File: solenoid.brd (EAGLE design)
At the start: 35.6 x 30.5 mm, 40 parts, among them Y1 ECS-80-S-4X

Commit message: Update solenoid.brd
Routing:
- net +3V3: track 59.1 -> 63.3 mm
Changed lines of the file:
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@@
 <wire x1="29.972" y1="12.148" x2="29.674" y2="12.148" width="0.254" layer="1"/>
 <wire x1="29.972" y1="10.922" x2="29.972" y2="12.148" width="0.254" layer="1"/>
-<wire x1="20.558" y1="19.288" x2="20.32" y2="19.05" width="0.254" layer="16"/>
-<wire x1="20.32" y1="19.05" x2="20.32" y2="18.542" width="0.254" layer="16"/>
-<via x="20.32" y="18.542" extent="1-16" drill="0.35"/>
-<wire x1="20.32" y1="18.542" x2="20.32" y2="18.034" width="0.254" layer="1"/>
-<wire x1="20.32" y1="18.034" x2="20.606" y2="17.748" width="0.254" layer="1"/>
+<via x="20.066" y="18.542" extent="1-16" drill="0.35"/>
+<wire x1="20.066" y1="18.542" x2="20.066" y2="18.288" width="0.254" layer="1"/>
+<wire x1="20.066" y1="18.288" x2="20.606" y2="17.748" width="0.254" layer="1"/>
 <wire x1="20.606" y1="17.748" x2="21.174" y2="17.748" width="0.254" layer="1"/>
 <wire x1="31.558" y1="10.506" x2="30.388" y2="10.506" width="0.254" layer="1"/>
@@
 <via x="20.0084" y="11.95728125" extent="1-16" drill="0.35"/>
 <wire x1="22.86" y1="15.976" x2="22.606" y2="15.722" width="0.254" layer="16"/>
-<wire x1="22.606" y1="15.722" x2="22.606" y2="14.058" width="0.254" layer="16"/>
+<wire x1="22.606" y1="15.722" x2="22.606" y2="14.986" width="0.254" layer="16"/>
+<wire x1="22.606" y1="14.058" x2="22.606" y2="14.986" width="0.254" layer="16"/>
 <wire x1="22.606" y1="14.058" x2="20.0084" y2="14.058" width="0.254" layer="16"/>
 <wire x1="20.0084" y1="14.058" x2="19.138" y2="14.058" width="0.254" layer="16"/>
@@
 <wire x1="10.834" y1="20.74" x2="12.446" y2="22.352" width="0.254" layer="1"/>
 <wire x1="12.446" y1="22.352" x2="18.542" y2="22.352" width="0.254" layer="1"/>
+<wire x1="22.606" y1="14.986" x2="21.971" y2="15.621" width="0.254" layer="16"/>
+<wire x1="21.971" y1="15.621" x2="21.336" y2="15.621" width="0.254" layer="16"/>
+<wire x1="21.336" y1="15.621" x2="20.955" y2="16.002" width="0.254" layer="16"/>
+<wire x1="20.955" y1="16.002" x2="20.955" y2="17.653" width="0.254" layer="16"/>
+<wire x1="20.955" y1="17.653" x2="20.066" y2="18.542" width="0.254" layer="16"/>
 </signal>
 <signal name="GPIO1">
@@
 <wire x1="33.258" y1="10.506" x2="33.288" y2="10.476" width="0.254" layer="1"/>
 <wire x1="33.288" y1="10.476" x2="33.288" y2="8.836" width="0.254" layer="1"/>
-<wire x1="33.288" y1="8.836" x2="33.288" y2="8.58286875" width="0.254" layer="1"/>
 <wire x1="32.931" y1="12.984" x2="33.258" y2="12.657" width="0.254" layer="1"/>
 <wire x1="33.258" y1="12.657" x2="33.258" y2="10.506" width="0.254" layer="1"/>
@@
 <wire x1="32.687" y1="15.2689125" x2="32.687" y2="12.984" width="0.254" layer="1"/>
 <wire x1="30.734" y1="6.604" x2="32.131" y2="6.604" width="0.254" layer="1"/>
+<wire x1="32.131" y1="6.604" x2="33.288" y2="7.761" width="0.254" layer="1"/>
 <wire x1="33.288" y1="7.761" x2="33.288" y2="8.836" width="0.254" layer="1"/>
-<wire x1="32.131" y1="6.604" x2="33.288" y2="7.761" width="0.254" layer="1"/>
 </signal>
 <signal name="SWDIO">

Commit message: Update solenoid.brd
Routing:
- net SWCLK: track 7.57 -> 13.3 mm
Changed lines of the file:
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@@
 <wire x1="21.174" y1="11.2179125" x2="20.399" y2="10.4429125" width="0.254" layer="1"/>
 <wire x1="21.174" y1="11.2179125" x2="21.174" y2="12.148" width="0.254" layer="1"/>
-<wire x1="20.399" y1="8.3284" x2="20.574" y2="8.1534" width="0.254" layer="1"/>
-<wire x1="20.574" y1="8.1534" x2="20.96328125" y2="8.1534" width="0.254" layer="1"/>
-<wire x1="20.96328125" y1="8.1534" x2="22.51268125" y2="6.604" width="0.254" layer="1"/>
+<wire x1="20.574" y1="8.1534" x2="20.399" y2="8.3284" width="0.254" layer="1"/>
 <wire x1="20.399" y1="10.4429125" x2="20.399" y2="8.3284" width="0.254" layer="1"/>
-<wire x1="22.51268125" y1="6.604" x2="23.114" y2="6.604" width="0.254" layer="1"/>
+<wire x1="21.971" y1="4.064" x2="21.717" y2="4.318" width="0.254" layer="1"/>
+<wire x1="21.717" y1="4.318" x2="21.717" y2="7.493" width="0.254" layer="1"/>
+<wire x1="21.717" y1="7.493" x2="21.0566" y2="8.1534" width="0.254" layer="1"/>
+<wire x1="21.0566" y1="8.1534" x2="20.574" y2="8.1534" width="0.254" layer="1"/>
+<wire x1="23.114" y1="4.445" x2="23.368" y2="4.191" width="0.254" layer="1"/>
+<wire x1="23.368" y1="4.191" x2="23.241" y2="4.064" width="0.254" layer="1"/>
+<wire x1="23.114" y1="6.604" x2="23.114" y2="4.445" width="0.254" layer="1"/>
+<wire x1="23.241" y1="4.064" x2="21.971" y2="4.064" width="0.254" layer="1"/>
 </signal>
 <signal name="OSC_IN">

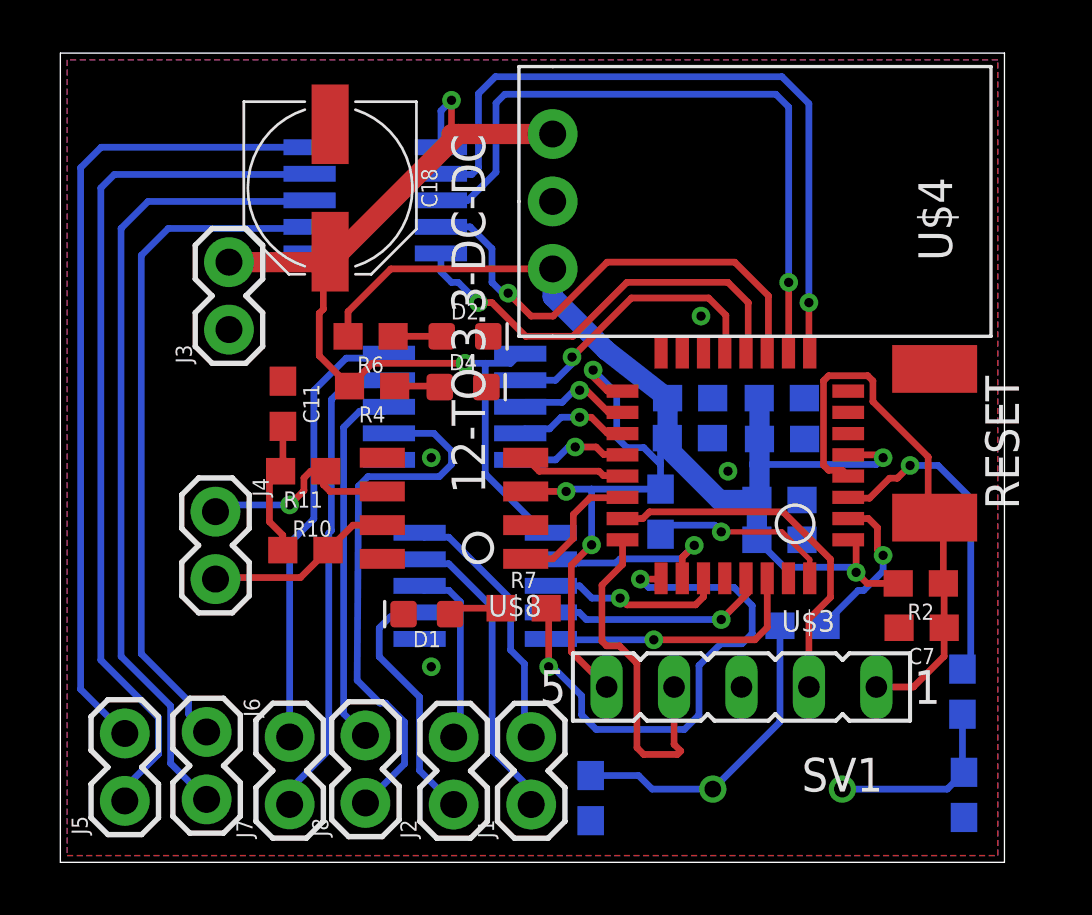
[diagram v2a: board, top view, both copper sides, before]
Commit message: small updates
finished making the wire impedances the same for oscillator and programming header, also made minor wire movements
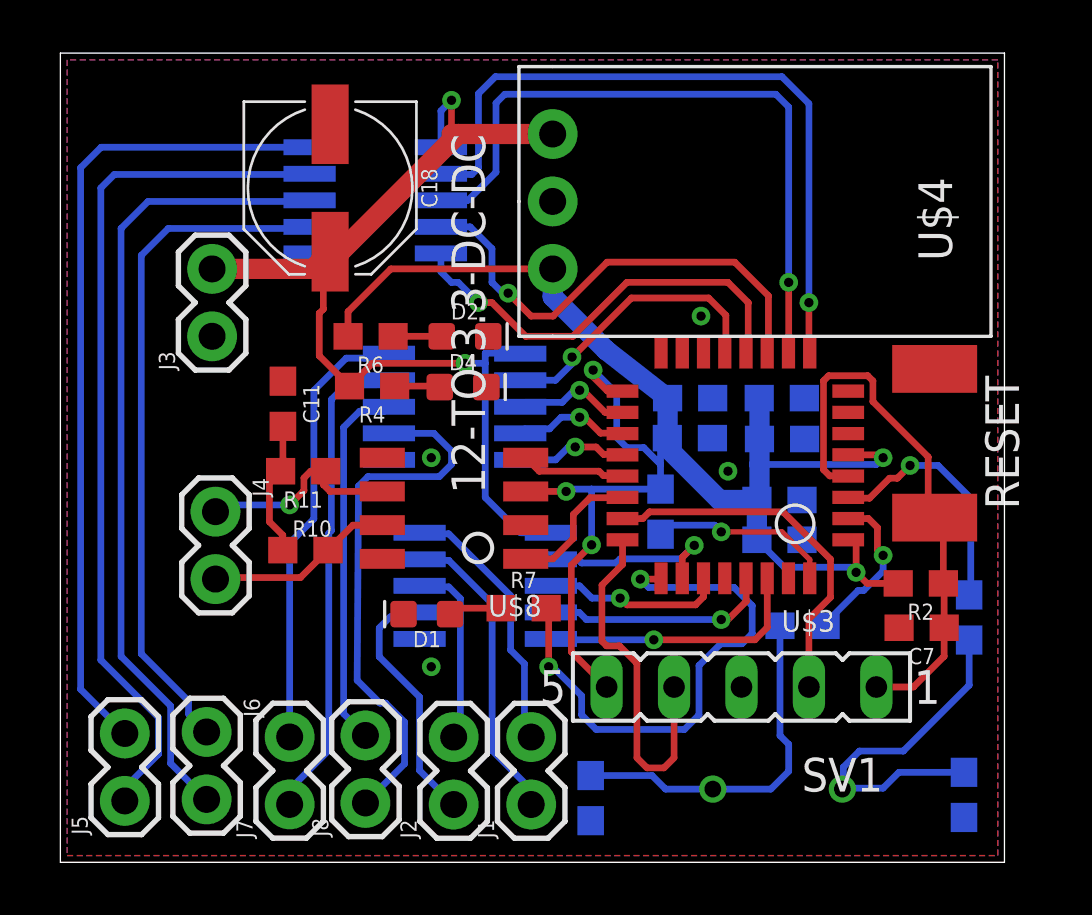
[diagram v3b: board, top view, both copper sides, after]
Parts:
- moved R1 2.81 mm to (34.2, 9.22)
- moved J3 0.68 mm to (5.71, 19.8)
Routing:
- net N$1: track 7.06 -> 13.4 mm
- net OSC_OUT: track 12.2 -> 9.32 mm
- net N$2: track 12.0 -> 13.6 mm
- net 12V: track 37.7 -> 39.2 mm

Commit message: Update solenoid.brd
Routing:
- net OSC_IN: track 6.05 -> 9.41 mm
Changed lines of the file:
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@@
 <contactref element="U$3" pad="PF0-OSC_IN"/>
 <contactref element="R3" pad="2"/>
-<wire x1="28.804" y1="8.91" x2="28.804" y2="8.992" width="0.254" layer="16"/>
-<wire x1="30.051" y1="10.239" x2="30.2549125" y2="10.239" width="0.254" layer="16"/>
 <wire x1="30.775" y1="12.609" x2="30.436" y2="12.948" width="0.254" layer="1"/>
 <wire x1="30.436" y1="12.948" x2="29.674" y2="12.948" width="0.254" layer="1"/>
-<wire x1="28.804" y1="8.992" x2="30.051" y2="10.239" width="0.254" layer="16"/>
-<wire x1="30.988" y1="10.9720875" x2="30.988" y2="11.562" width="0.254" layer="16"/>
+<wire x1="28.804" y1="8.91" x2="28.9259125" y2="8.91" width="0.254" layer="16"/>
 <via x="30.988" y="11.562" extent="1-16" drill="0.35"/>
 <wire x1="30.988" y1="11.562" x2="30.775" y2="11.775" width="0.254" layer="1"/>
 <wire x1="30.775" y1="11.775" x2="30.775" y2="12.609" width="0.254" layer="1"/>
-<wire x1="30.2549125" y1="10.239" x2="30.988" y2="10.9720875" width="0.254" layer="16"/>
+<wire x1="30.988" y1="11.562" x2="31.501" y2="11.049" width="0.254" layer="16"/>
+<wire x1="31.501" y1="11.049" x2="32.004" y2="11.049" width="0.254" layer="16"/>
+<wire x1="32.004" y1="11.049" x2="32.131" y2="10.922" width="0.254" layer="16"/>
+<wire x1="28.824" y1="8.89" x2="28.804" y2="8.91" width="0.254" layer="16"/>
+<wire x1="32.131" y1="10.922" x2="32.385" y2="10.668" width="0.254" layer="16"/>
+<wire x1="32.385" y1="10.668" x2="32.385" y2="9.271" width="0.254" layer="16"/>
+<wire x1="32.385" y1="9.271" x2="32.004" y2="8.89" width="0.254" layer="16"/>
+<wire x1="32.004" y1="8.89" x2="28.824" y2="8.89" width="0.254" layer="16"/>
 </signal>
 <signal name="OSC_OUT">

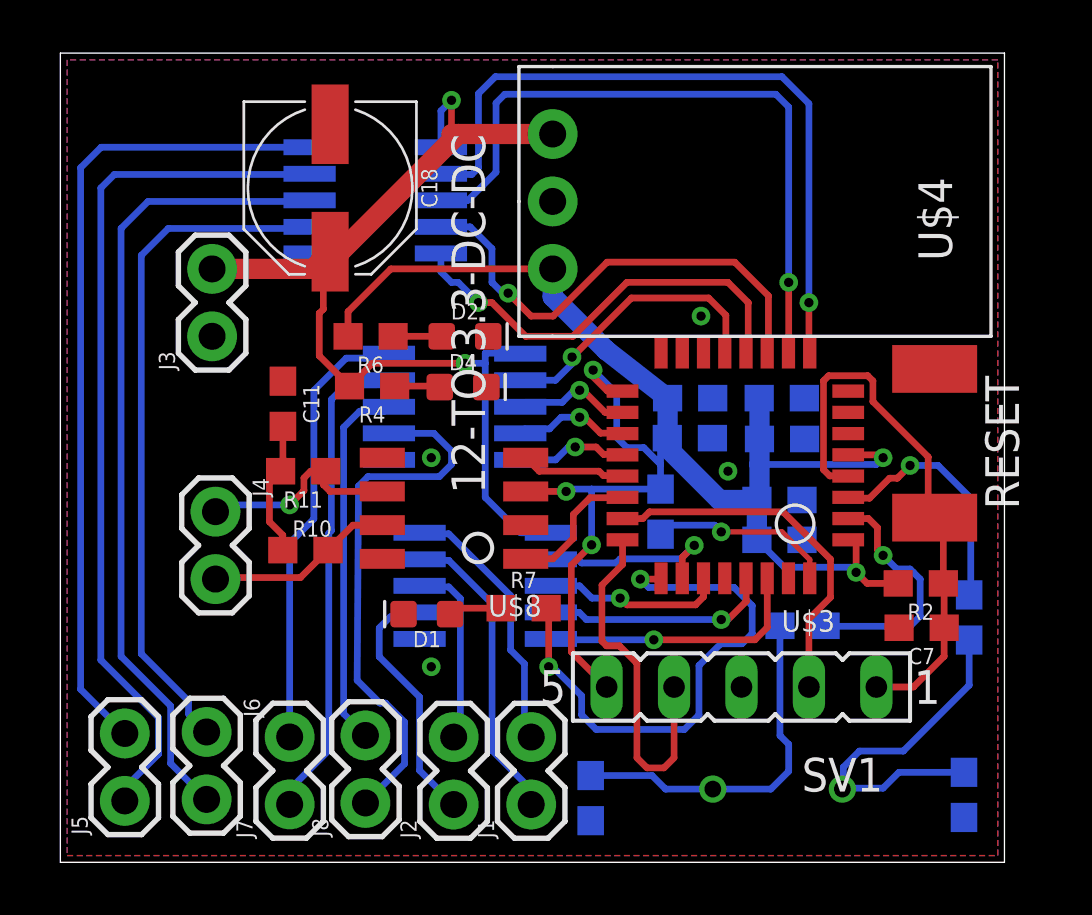
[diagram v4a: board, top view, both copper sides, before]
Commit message: added standoff, moved around some header
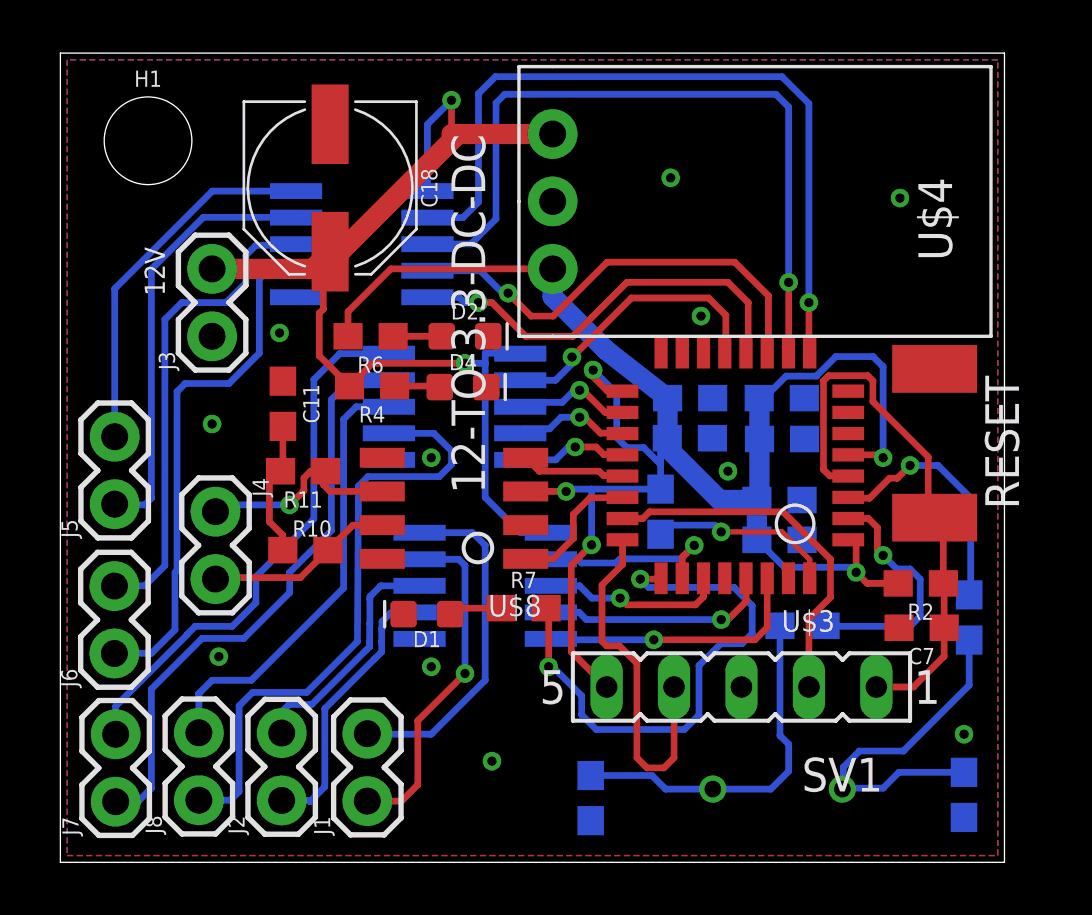
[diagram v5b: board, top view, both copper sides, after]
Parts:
- added H1: STAND-OFF, SparkFun-Hardware:STAND-OFF
- moved J5 11.2 mm to (2.04, 13.5)
- moved J7 6.55 mm to (2.08, 2.28)
- moved J2 6.48 mm to (8.34, 2.33)
- moved J8 6.27 mm to (5.22, 2.34)
- moved J1 6.17 mm to (11.6, 2.31)
- moved J6 4.56 mm to (2.04, 7.87), turned to 90 degrees
- moved U$5 1.73 mm to (11.4, 23.3)
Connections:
- removed net SOL7_1: J7.2, U$6.OUT1
- removed net SOL7_2: J7.1, U$6.OUT2
- removed net SOL8_1: J8.2, U$6.OUT3
- removed net SOL8_2: J8.1, U$6.OUT4
- new net SOL3_1: J5.2, U$5.OUT1
- new net SOL3_2: J5.1, U$5.OUT2
- new net SOL4_1: J6.2, U$5.OUT3
- new net SOL4_2: J6.1, U$5.OUT4
- net SOL5_1: now also J7.2, U$6.OUT1; no longer J5.2, U$5.OUT1
- net SOL5_2: now also J7.1, U$6.OUT2; no longer J5.1, U$5.OUT2
- net SOL6_1: now also J8.2, U$6.OUT3; no longer J6.2, U$5.OUT3
- net SOL6_2: now also J8.1, U$6.OUT4; no longer J6.1, U$5.OUT4
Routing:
- net SOL8_2: track 20.4 -> 0.00 mm
- net SOL4_2: track 0.00 -> 19.7 mm
- net SOL7_2: track 18.4 -> 0.00 mm
- net SOL4_1: track 0.00 -> 18.2 mm
- net SOL7_1: track 16.8 -> 0.00 mm
- net SOL3_2: track 0.00 -> 16.4 mm
- net SOL8_1: track 14.0 -> 0.00 mm
- net SOL3_1: track 0.00 -> 13.9 mm
- net SOL6_1: track 30.4 -> 16.8 mm
- net SOL5_1: track 30.9 -> 20.5 mm
- net SOL5_2: track 32.6 -> 22.4 mm
- net +3V3: track 63.3 -> 67.5 mm
- net SOL1_1: track 10.1 -> 13.0 mm
- net SOL6_2: track 25.8 -> 23.2 mm
- net GPIO9: track 25.7 -> 28.0 mm
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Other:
- board text added: "12V"

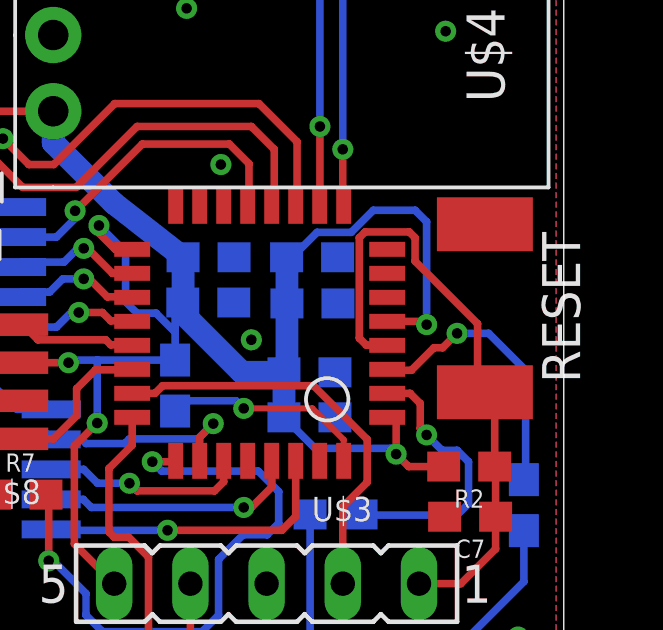
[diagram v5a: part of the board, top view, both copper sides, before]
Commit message: Solenoid v1
Final changes to capacitor and few small changes
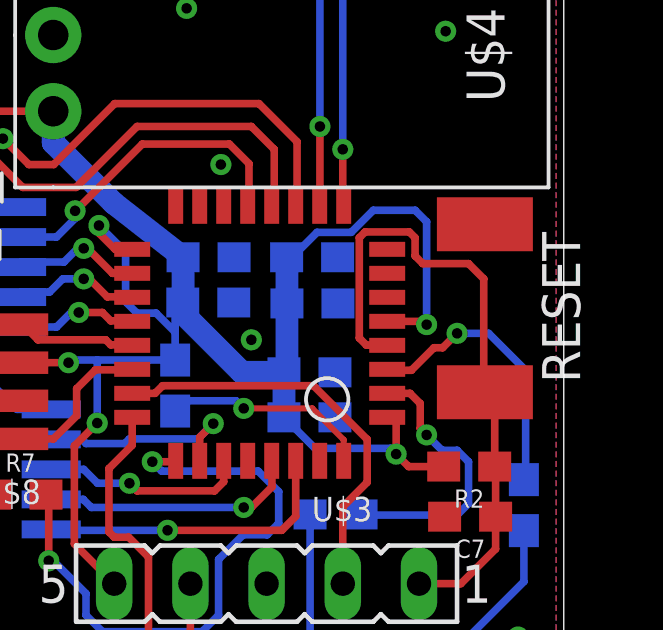
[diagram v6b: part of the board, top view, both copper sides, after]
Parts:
- C3, C4, C6: value 4.7uF -> 100nF
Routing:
- net NRST: track 21.1 -> 22.1 mm
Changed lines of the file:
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@@
 <?xml version="1.0" encoding="utf-8"?>
 <!DOCTYPE eagle SYSTEM "eagle.dtd">
-<eagle version="9.3.2">
+<eagle version="9.1.3">
 <drawing>
 <settings>
@@
 <attribute name="VALUE" x="23.72" y="18.246" size="0.6096" layer="28" font="vector" ratio="20" rot="MR180" align="top-center"/>
 </element>
-<element name="C3" library="SparkFun-Capacitors" library_urn="urn:adsk.eagle:library:510" package="0603" package3d_urn="urn:adsk.eagle:package:37414/1" value="4.7uF" x="27.084" y="13.648" smashed="yes" rot="MR180">
+<element name="C3" library="SparkFun-Capacitors" library_urn="urn:adsk.eagle:library:510" package="0603" package3d_urn="urn:adsk.eagle:package:37414/1" value="100nF" x="27.084" y="13.648" smashed="yes" rot="MR180">
 <attribute name="NAME" x="27.084" y="12.886" size="0.6096" layer="26" font="vector" ratio="20" rot="MR180" align="bottom-center"/>
 <attribute name="PROD_ID" value="CAP-08280" x="62.644" y="65.718" size="1.778" layer="28" rot="MR180" display="off"/>
 <attribute name="VALUE" x="27.084" y="14.41" size="0.6096" layer="28" font="vector" ratio="20" rot="MR180" align="top-center"/>
 </element>
-<element name="C4" library="SparkFun-Capacitors" library_urn="urn:adsk.eagle:library:510" package="0603" package3d_urn="urn:adsk.eagle:package:37414/1" value="4.7uF" x="23.71" y="15.976" smashed="yes" rot="MR180">
+<element name="C4" library="SparkFun-Capacitors" library_urn="urn:adsk.eagle:library:510" package="0603" package3d_urn="urn:adsk.eagle:package:37414/1" value="100nF" x="23.71" y="15.976" smashed="yes" rot="MR180">
 <attribute name="NAME" x="23.71" y="15.214" size="0.6096" layer="26" font="vector" ratio="20" rot="MR180" align="bottom-center"/>
 <attribute name="PROD_ID" value="CAP-08280" x="63.08" y="68.046" size="1.778" layer="28" rot="MR180" display="off"/>
@@
 <attribute name="VALUE" x="27.172" y="18.246" size="0.6096" layer="28" font="vector" ratio="20" rot="MR180" align="top-center"/>
 </element>
-<element name="C6" library="SparkFun-Capacitors" library_urn="urn:adsk.eagle:library:510" package="0603" package3d_urn="urn:adsk.eagle:package:37414/1" value="4.7uF" x="27.182" y="15.946" smashed="yes" rot="MR180">
+<element name="C6" library="SparkFun-Capacitors" library_urn="urn:adsk.eagle:library:510" package="0603" package3d_urn="urn:adsk.eagle:package:37414/1" value="100nF" x="27.182" y="15.946" smashed="yes" rot="MR180">
 <attribute name="NAME" x="27.182" y="15.184" size="0.6096" layer="26" font="vector" ratio="20" rot="MR180" align="bottom-center"/>
 <attribute name="PROD_ID" value="CAP-08280" x="74.172" y="68.016" size="1.778" layer="28" rot="MR180" display="off"/>
@@
 <wire x1="28.7438" y1="18.134775" x2="28.937225" y2="18.3282" width="0.254" layer="1"/>
 <wire x1="28.937225" y1="18.3282" x2="30.410775" y2="18.3282" width="0.254" layer="1"/>
-<wire x1="30.410775" y1="18.3282" x2="30.6042" y2="18.134775" width="0.254" layer="1"/>
 <wire x1="28.7438" y1="14.7918" x2="28.7438" y2="18.134775" width="0.254" layer="1"/>
-<wire x1="30.6042" y1="18.134775" x2="30.6042" y2="17.3517125" width="0.254" layer="1"/>
 <wire x1="29.674" y1="14.548" x2="29.6678" y2="14.5542" width="0.254" layer="1"/>
 <wire x1="29.6678" y1="14.5542" x2="28.9814" y2="14.5542" width="0.254" layer="1"/>
-<wire x1="30.6042" y1="17.3517125" x2="32.687" y2="15.2689125" width="0.254" layer="1"/>
-<wire x1="32.687" y1="15.2689125" x2="32.687" y2="12.984" width="0.254" layer="1"/>
 <wire x1="30.734" y1="6.604" x2="32.131" y2="6.604" width="0.254" layer="1"/>
 <wire x1="32.131" y1="6.604" x2="33.288" y2="7.761" width="0.254" layer="1"/>
 <wire x1="33.288" y1="7.761" x2="33.288" y2="8.836" width="0.254" layer="1"/>
+<wire x1="30.410775" y1="18.3282" x2="30.6042" y2="18.134775" width="0.254" layer="1"/>
+<wire x1="30.6042" y1="18.134775" x2="30.6042" y2="17.5288" width="0.254" layer="1"/>
+<wire x1="32.385" y1="17.272" x2="32.893" y2="16.764" width="0.254" layer="1"/>
+<wire x1="32.893" y1="16.764" x2="32.893" y2="13.022" width="0.254" layer="1"/>
+<wire x1="32.893" y1="13.022" x2="32.931" y2="12.984" width="0.254" layer="1"/>
+<wire x1="30.6042" y1="17.5288" x2="30.861" y2="17.272" width="0.254" layer="1"/>
+<wire x1="30.861" y1="17.272" x2="32.385" y2="17.272" width="0.254" layer="1"/>
 </signal>
 <signal name="SWDIO">

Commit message: put on bmp
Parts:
- C5: value 4.7uF -> 0.01uF
- C6: value 100nF -> 1uF
